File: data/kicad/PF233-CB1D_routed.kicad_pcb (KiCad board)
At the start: 6 copper layers, 78 x 77.2 mm, 62 parts, among them M5 5 V 1.5 A switching module, U1 Pico 2 W

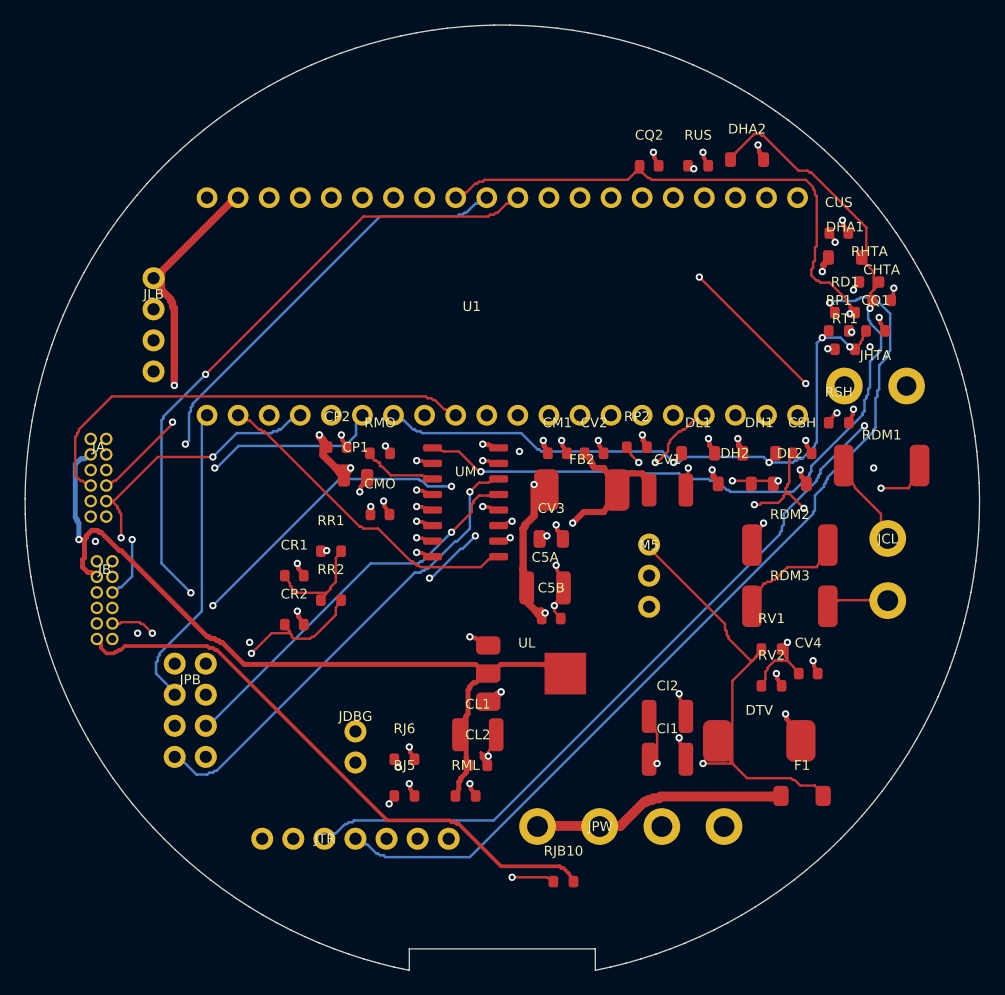
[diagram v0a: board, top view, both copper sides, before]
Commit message: WIP: CB1D-C2 dual-source gyro land (BMI270 / LSM6DSO, pins 2-3 to VDDIO), LSM6DSO datasheet logged, gyro cluster re-placed for escape; CB1D re-route running
Co-Authored-By: Claude Opus 5.5 <noreply@anthropic.com>
Claude-Session: https://claude.ai/code/session_01FX4DWSYYjMCFGGA6gmha65
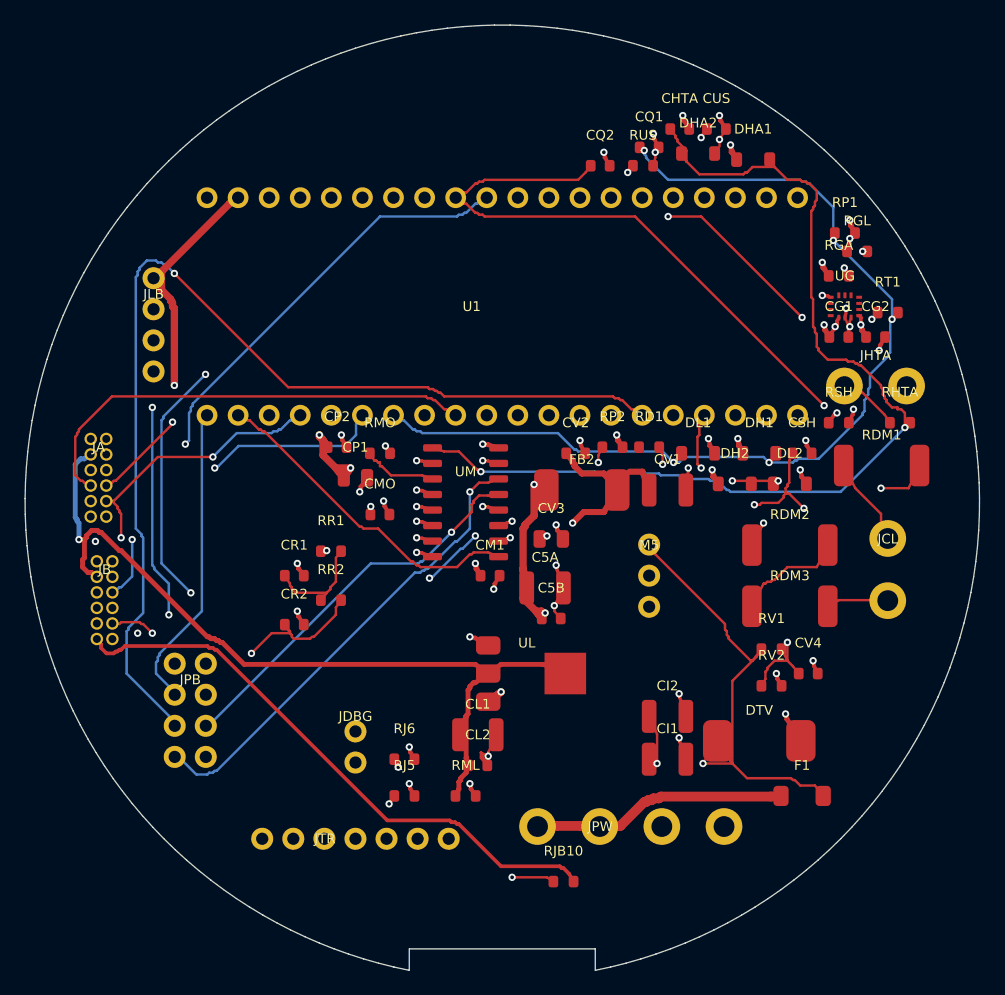
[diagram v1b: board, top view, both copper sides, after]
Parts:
- added CG1: 100n, Capacitor_SMD:C_0603_1608Metric, F.Cu at (127.5, 86.5)
- added CG2: 100n, Capacitor_SMD:C_0603_1608Metric, F.Cu at (130.5, 86.5)
- added RGA: 4k7, Resistor_SMD:R_0603_1608Metric, F.Cu at (127.5, 81.5)
- added RGL: 4k7, Resistor_SMD:R_0603_1608Metric, F.Cu at (129.0, 79.5)
- added UG: BMI270, PF233:BMI270_LGA-14_2.5x3.0mm, F.Cu at (128.0, 84.0)
- moved CQ1 23.8 mm to (112.0, 71.0)
- moved CHTA 21.6 mm to (114.5, 69.5)
- moved RD1 19.4 mm to (112.0, 95.5)
- moved CUS 13.1 mm to (117.5, 69.5)
- moved RHTA 11.8 mm to (132.5, 93.5)
- moved CM1 11.4 mm to (99.0, 106.0)
- moved DHA1 11.0 mm to (120.5, 72.0)
- moved RP1 8.02 mm to (128.0, 78.0)
- moved RT1 4.61 mm to (131.5, 84.5)
- moved RUS 4.50 mm to (111.5, 72.5)
- moved DHA2 4.03 mm to (116.0, 71.5)
- moved CQ2 4.00 mm to (108.0, 72.5)
- moved RP2 2.00 mm to (109.0, 95.5)
- moved CV2 1.50 mm to (106.0, 96.0)
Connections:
- U1 pad 21: (no net) -> GYR_SDA
- U1 pad 22: (no net) -> GYR_SCL
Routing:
- net DIAL_EXT: track 76.1 -> 0.00 mm, vias 1 -> 0
- net FAULT1_N: track 54.9 -> 86.4 mm, vias 3 -> 1
- net TRIG_IN: track 57.5 -> 86.0 mm, vias 4 -> 5
- net UMB_SHLD: track 102.3 -> 88.5 mm, vias 3 -> 4
- net P3V3: track 16.9 -> 29.8 mm, vias 8 -> 12
- net HTA_IN: track 75.1 -> 86.7 mm
- net GYR_SCL: track 0.00 -> 9.61 mm, vias 0 -> 1
- net GYR_SDA: track 0.00 -> 8.76 mm, vias 0 -> 1
- net GND: track 108.7 -> 116.0 mm, vias 39 -> 43
- net TRIG_EXT: track 78.6 -> 85.3 mm, vias 2 -> 1
- net HTA_P: track 10.0 -> 4.92 mm, vias 1 -> 0
- net VBUS_SENSE: track 75.9 -> 79.2 mm, vias 4 -> 3
- net REF_PWM1: track 37.6 -> 39.9 mm
- net +5VA: track 65.5 -> 66.9 mm
- net DIAL_IN: track 77.7 -> 76.4 mm, vias 4 -> 5

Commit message: WIP (NOT signed off): data published by the first close-out sign-off run, which had 5 FAIL (CB1D-C2 / AU1 fine-pitch clearance); superseded by the rerun in progress
Co-Authored-By: Claude Opus 5.5 <noreply@anthropic.com>
Claude-Session: https://claude.ai/code/session_01FX4DWSYYjMCFGGA6gmha65
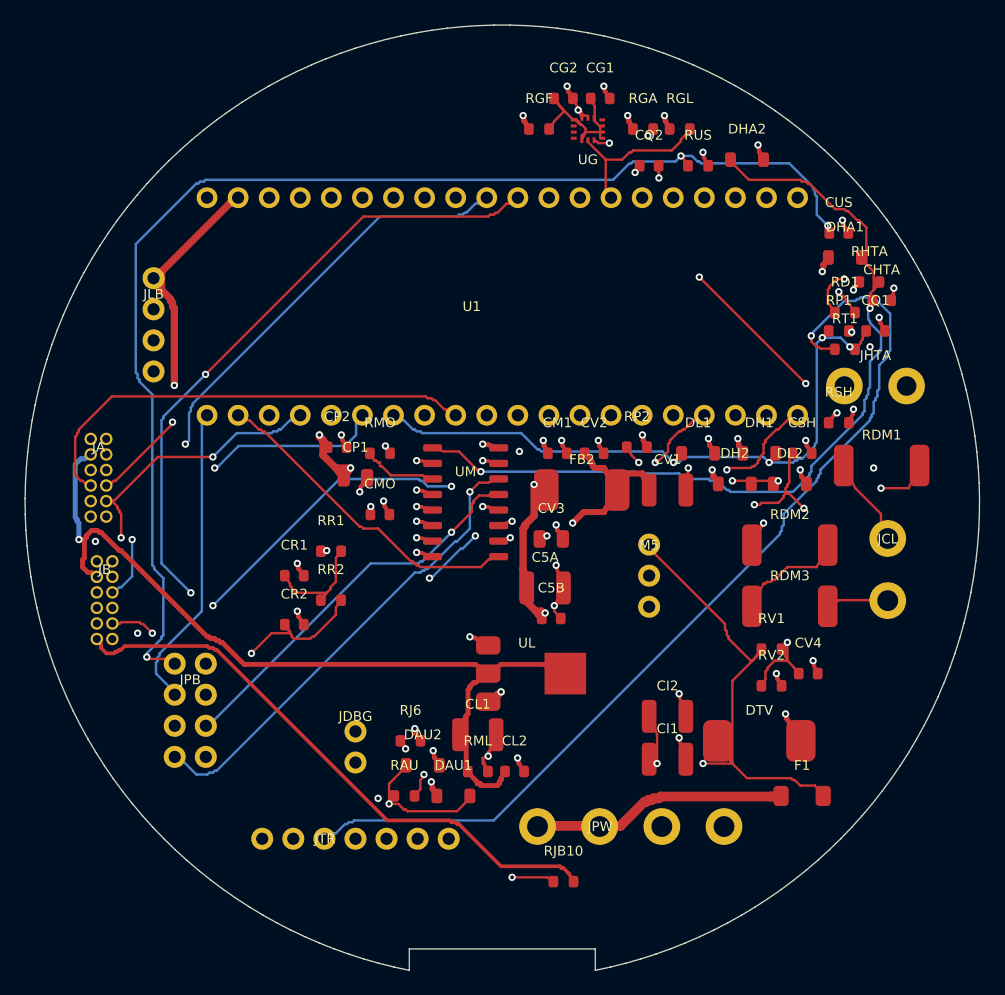
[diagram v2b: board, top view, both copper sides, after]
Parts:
- removed RJ5: 0R DNP, Resistor_SMD:R_0603_1608Metric
- added DAU1: BAS16, Diode_SMD:D_SOD-123, F.Cu at (96.0, 124.0)
- added DAU2: BAS16, Diode_SMD:D_SOD-123, F.Cu at (93.5, 121.5)
- added RAU: 100R, Resistor_SMD:R_0603_1608Metric, F.Cu at (92.0, 124.0)
- added RGF: 10R, Resistor_SMD:R_0603_1608Metric, F.Cu at (103.0, 69.5)
- JTR: value Handle: +3V3 GND TRIG DIAL JOYX JOYY SHLD -> Handle: +3V3 GND TRIG DIAL AUD_LINK - SHLD
- moved CG2 32.1 mm to (105.0, 67.0)
- moved CG1 27.6 mm to (108.0, 67.0)
- moved UG 25.5 mm to (107.0, 69.5), turned to 180 degrees
- moved CQ1 23.8 mm to (130.5, 86.0)
- moved CHTA 21.6 mm to (131.0, 83.5)
- moved RGA 20.0 mm to (111.5, 69.5)
- moved RD1 19.4 mm to (128.0, 84.5)
- moved RGL 17.6 mm to (114.5, 69.5)
- moved CUS 13.1 mm to (127.5, 78.0)
- moved RHTA 11.8 mm to (130.0, 82.0)
- moved CM1 11.4 mm to (104.5, 96.0)
- moved DHA1 11.0 mm to (128.0, 80.0)
- moved RP1 8.02 mm to (127.5, 86.0)
- moved RT1 4.61 mm to (128.0, 87.5)
- moved RUS 4.50 mm to (116.0, 72.5)
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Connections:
- CG1 pad 1: P3V3 -> UG_VIO
- CG2 pad 1: P3V3 -> UG_VIO
- JTR pad 5: JTR5_OPT -> AUD_LINK
- U1 pad 20: (no net) -> AUD_PIO
- U1 pad 21: GYR_SDA -> (no net)
- U1 pad 22: GYR_SCL -> (no net)
- U1 pad 26: (no net) -> GYR_SDA
- U1 pad 27: (no net) -> GYR_SCL
- UG pad 1: GND -> UG_VIO
- UG pad 12: P3V3 -> UG_VIO
- UG pad 2: UG_ASDX_NC -> UG_VIO
- UG pad 3: UG_ASCX_NC -> UG_VIO
- UG pad 5: P3V3 -> UG_VIO
- UG pad 8: P3V3 -> UG_VIO
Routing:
- net DIAL_EXT: track 0.00 -> 76.8 mm, vias 0 -> 2
- net AUD_PIO: track 0.00 -> 46.8 mm, vias 0 -> 2
- net FAULT1_N: track 86.4 -> 54.9 mm, vias 1 -> 3
- net TRIG_IN: track 86.0 -> 57.5 mm, vias 5 -> 4
- net AUD_LINK: track 0.00 -> 17.2 mm, vias 0 -> 1
- net UMB_SHLD: track 88.5 -> 103.9 mm, vias 4 -> 3
- net UG_VIO: track 0.00 -> 13.4 mm
- net HTA_IN: track 86.7 -> 73.4 mm
- net HTA_P: track 4.92 -> 10.0 mm, vias 0 -> 1
- net TRIG_EXT: track 85.3 -> 80.2 mm
- net JTR5_OPT: track 4.47 -> 0.00 mm, vias 1 -> 0
- net GYR_SCL: track 9.61 -> 13.4 mm, vias 1 -> 0
- net VBUS_SENSE: track 79.2 -> 75.9 mm, vias 3 -> 4
- net P3V3: track 29.8 -> 26.7 mm
- net +3V3D: track 72.7 -> 75.0 mm
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
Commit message: WIP (NOT signed off): data published by the second close-out run (8 FAIL: 3 opens on CB1D-C2 / AU1 under the exact fine-zone keep-out); third run in progress
Co-Authored-By: Claude Opus 5.5 <noreply@anthropic.com>
Claude-Session: https://claude.ai/code/session_01FX4DWSYYjMCFGGA6gmha65
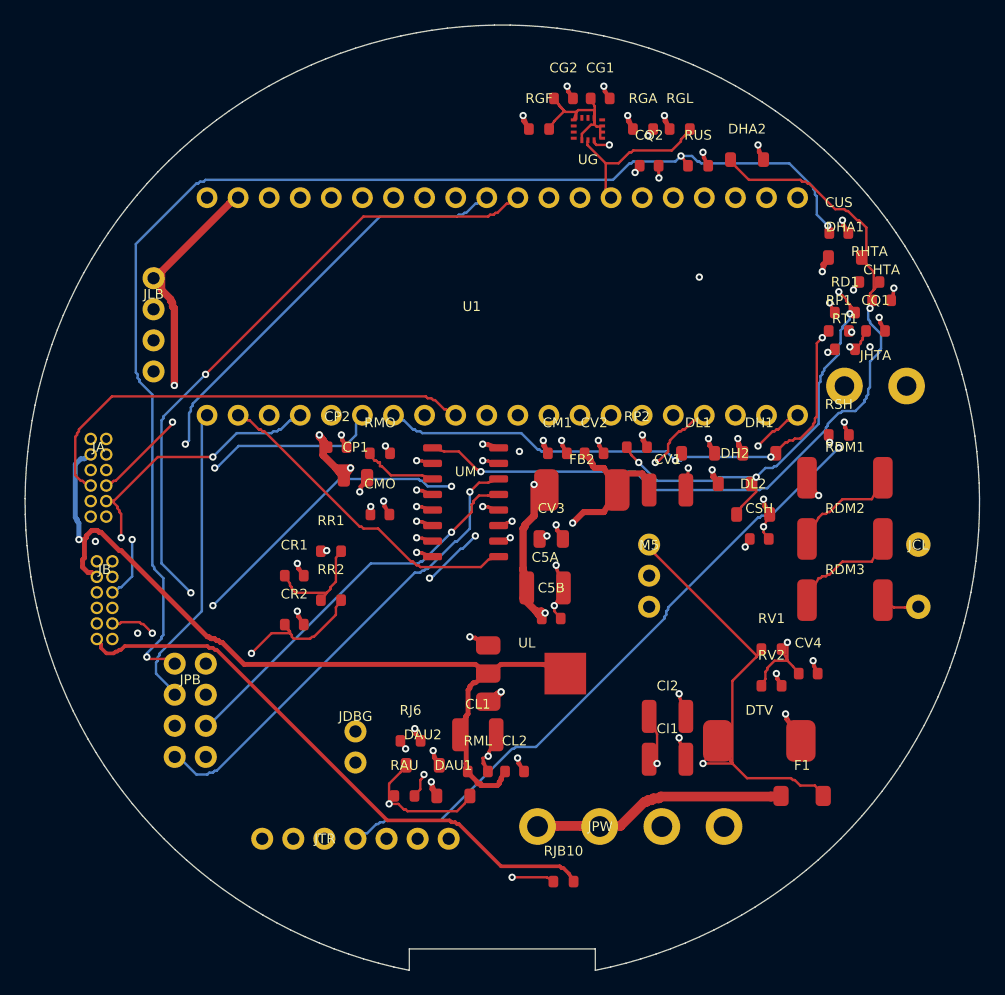
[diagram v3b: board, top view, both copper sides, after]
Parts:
- removed the JCL at (131.5, 105.5)
- removed the JLB at (71.5, 85.5)
- added JCL: Coil taps from TXJ1: COIL_B (drain side), COIL_A (VBUS side), Connector:Solder_holes_AWG22_1x2_P5.08mm, F.Cu at (134.0, 106.0)
- added JLB: to LB1: +5V, LED_IN, LED_CLK, GND, Connector:Wire_pads_1x4_P2.54mm, F.Cu at (71.5, 85.5)
- moved CSH 7.83 mm to (121.0, 103.0)
- moved RDM2 4.53 mm to (128.0, 103.0)
- moved RDM3 4.53 mm to (128.0, 108.0)
- moved DL2 3.91 mm to (120.5, 101.0)
- moved RDM1 3.16 mm to (128.0, 98.0)
- moved RSH 1.00 mm to (127.5, 94.5)
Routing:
- net TRIG_EXT: track 80.2 -> 64.4 mm
- net DM1: track 19.2 -> 8.93 mm, vias 2 -> 0
- net SHIELD: track 57.3 -> 48.3 mm, vias 3 -> 2
- net COIL_B: track 7.16 -> 13.2 mm, vias 0 -> 1
- net DIAL_EXT: track 76.8 -> 71.0 mm
- net GND: track 117.9 -> 114.5 mm, vias 42 -> 41
- net VBUS_SENSE: track 75.9 -> 72.7 mm, vias 4 -> 2
- net TRIG_IN: track 57.5 -> 54.4 mm
- net COIL_A: track 5.03 -> 3.08 mm
- net DIAL_IN: track 78.2 -> 79.9 mm
- net UG_VIO: track 13.4 -> 14.9 mm
- net MUX_S1: track 55.1 -> 54.1 mm
- net MUX_S0: track 53.7 -> 52.7 mm
- net HTA_IN: track 73.4 -> 72.6 mm
- net AUD_PIO: track 46.8 -> 46.1 mm
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
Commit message: WIP (NOT signed off): data written by the close-out runs in progress (fourth run with the 0.15 mm fine-pitch neck-down is running)
Co-Authored-By: Claude Opus 5.5 <noreply@anthropic.com>
Claude-Session: https://claude.ai/code/session_01FX4DWSYYjMCFGGA6gmha65
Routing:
- net GND: track 114.5 -> 117.3 mm, vias 41 -> 42
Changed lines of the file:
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@@
   (gr_line (start 107.600 136.500) (end 92.400 136.500) (stroke (width 0.1) (type default)) (layer "Edge.Cuts"))
   (gr_line (start 92.400 136.500) (end 92.400 138.252) (stroke (width 0.1) (type default)) (layer "Edge.Cuts"))
+  (segment (start 106.9500 68.7000) (end 106.9500 69.3000) (width 0.2) (layer "F.Cu") (net 15))
+  (segment (start 106.9500 69.3000) (end 107.0000 68.5875) (width 0.2) (layer "F.Cu") (net 15))
+  (segment (start 106.5000 68.4000) (end 106.5000 67.9500) (width 0.2) (layer "F.Cu") (net 15))
+  (segment (start 106.5000 67.9500) (end 106.3500 67.8000) (width 0.2) (layer "F.Cu") (net 15))
+  (segment (start 106.3500 67.8000) (end 105.7750 67.0000) (width 0.2) (layer "F.Cu") (net 15))
   (segment (start 108.8900 75.1100) (end 108.4500 74.4000) (width 0.2) (layer "F.Cu") (net 16))
   (segment (start 108.4500 74.4000) (end 108.4500 72.3000) (width 0.2) (layer "F.Cu") (net 16))
@@
   (segment (start 108.0000 69.7500) (end 108.0000 69.3000) (width 0.2) (layer "F.Cu") (net 50))
   (segment (start 108.0000 69.3000) (end 107.7000 69.3000) (width 0.2) (layer "F.Cu") (net 50))
-  (segment (start 107.7000 69.3000) (end 107.5500 69.1500) (width 0.2) (layer "F.Cu") (net 50))
+  (segment (start 107.7000 69.3000) (end 107.7000 69.1500) (width 0.2) (layer "F.Cu") (net 50))
+  (segment (start 107.7000 69.1500) (end 107.5500 69.1500) (width 0.2) (layer "F.Cu") (net 50))
   (segment (start 107.5500 69.1500) (end 107.5500 68.7000) (width 0.2) (layer "F.Cu") (net 50))
   (segment (start 107.5500 68.7000) (end 107.5500 67.6500) (width 0.2) (layer "F.Cu") (net 50))
   (segment (start 107.5500 67.6500) (end 107.2250 67.0000) (width 0.2) (layer "F.Cu") (net 50))
-  (segment (start 107.5000 68.5875) (end 107.5500 69.1500) (width 0.2) (layer "F.Cu") (net 50))
-  (segment (start 107.5500 69.1500) (end 107.2500 69.1500) (width 0.2) (layer "F.Cu") (net 50))
-  (segment (start 107.2500 69.1500) (end 106.5000 69.9000) (width 0.2) (layer "F.Cu") (net 50))
-  (segment (start 106.5000 69.9000) (end 106.5000 70.2000) (width 0.2) (layer "F.Cu") (net 50))
-  (segment (start 107.5000 68.5875) (end 107.5500 67.9500) (width 0.2) (layer "F.Cu") (net 50))
-  (segment (start 107.5500 67.9500) (end 106.2000 67.9500) (width 0.2) (layer "F.Cu") (net 50))
-  (segment (start 106.2000 67.9500) (end 106.0500 68.1000) (width 0.2) (layer "F.Cu") (net 50))
-  (segment (start 106.0500 68.1000) (end 106.0500 68.7000) (width 0.2) (layer "F.Cu") (net 50))
-  (segment (start 105.8375 68.7500) (end 106.0500 68.1000) (width 0.2) (layer "F.Cu") (net 50))
-  (segment (start 106.0500 68.1000) (end 105.1500 68.1000) (width 0.2) (layer "F.Cu") (net 50))
-  (segment (start 105.1500 68.1000) (end 104.7000 67.6500) (width 0.2) (layer "F.Cu") (net 50))
-  (segment (start 104.7000 67.6500) (end 104.2250 67.0000) (width 0.2) (layer "F.Cu") (net 50))
-  (segment (start 104.2250 67.0000) (end 105.0000 67.9500) (width 0.2) (layer "F.Cu") (net 50))
-  (segment (start 105.0000 67.9500) (end 105.0000 68.1000) (width 0.2) (layer "F.Cu") (net 50))
-  (segment (start 105.0000 68.1000) (end 104.2500 68.8500) (width 0.2) (layer "F.Cu") (net 50))
+  (segment (start 107.2250 67.0000) (end 107.5500 67.6500) (width 0.2) (layer "F.Cu") (net 50))
+  (segment (start 107.5500 67.6500) (end 107.5500 66.9000) (width 0.2) (layer "F.Cu") (net 50))
+  (segment (start 107.5500 66.9000) (end 106.6500 66.0000) (width 0.2) (layer "F.Cu") (net 50))
+  (segment (start 106.6500 66.0000) (end 106.5000 66.0000) (width 0.2) (layer "F.Cu") (net 50))
+  (segment (start 106.5000 66.0000) (end 106.3500 65.8500) (width 0.2) (layer "F.Cu") (net 50))
+  (segment (start 106.3500 65.8500) (end 105.0000 65.8500) (width 0.2) (layer "F.Cu") (net 50))
+  (segment (start 105.0000 65.8500) (end 104.8500 66.0000) (width 0.2) (layer "F.Cu") (net 50))
+  (segment (start 104.8500 66.0000) (end 104.8500 66.1500) (width 0.2) (layer "F.Cu") (net 50))
+  (segment (start 104.8500 66.1500) (end 104.7000 66.3000) (width 0.2) (layer "F.Cu") (net 50))
+  (segment (start 104.7000 66.3000) (end 104.7000 66.4500) (width 0.2) (layer "F.Cu") (net 50))
+  (segment (start 104.7000 66.4500) (end 104.2250 67.0000) (width 0.2) (layer "F.Cu") (net 50))
+  (segment (start 104.2250 67.0000) (end 104.7000 66.4500) (width 0.2) (layer "F.Cu") (net 50))
+  (segment (start 104.7000 66.4500) (end 104.7000 68.4000) (width 0.2) (layer "F.Cu") (net 50))
+  (segment (start 104.7000 68.4000) (end 104.2500 68.8500) (width 0.2) (layer "F.Cu") (net 50))
   (segment (start 104.2500 68.8500) (end 103.8250 69.5000) (width 0.2) (layer "F.Cu") (net 50))
+  (segment (start 104.7000 68.4000) (end 105.4500 68.4000) (width 0.2) (layer "F.Cu") (net 50))
+  (segment (start 105.4500 68.4000) (end 105.7500 68.7000) (width 0.2) (layer "F.Cu") (net 50))
   (segment (start 88.9500 98.0000) (end 88.3500 98.7000) (width 0.2) (layer "F.Cu") (net 15))
   (segment (start 88.3500 98.7000) (end 88.3500 99.1500) (width 0.2) (layer "F.Cu") (net 15))
@@
   (segment (start 108.3000 66.4500) (end 108.3000 66.0000) (width 0.2) (layer "F.Cu") (net 15))
   (segment (start 108.3000 66.0000) (end 108.7750 67.0000) (width 0.2) (layer "F.Cu") (net 15))
-  (segment (start 105.7750 67.0000) (end 105.3000 66.4500) (width 0.2) (layer "F.Cu") (net 15))
-  (segment (start 105.3000 66.4500) (end 105.3000 66.0000) (width 0.2) (layer "F.Cu") (net 15))
-  (segment (start 105.3000 66.0000) (end 105.7750 67.0000) (width 0.2) (layer "F.Cu") (net 15))
+  (segment (start 105.7750 67.0000) (end 106.2000 67.6500) (width 0.2) (layer "F.Cu") (net 15))
+  (segment (start 106.2000 67.6500) (end 106.2000 68.1000) (width 0.2) (layer "F.Cu") (net 15))
+  (segment (start 106.2000 68.1000) (end 106.5000 68.5875) (width 0.2) (layer "F.Cu") (net 15))
   (segment (start 99.7000 95.5550) (end 98.8500 95.2500) (width 0.3) (layer "F.Cu") (net 31))
   (segment (start 98.8500 95.2500) (end 98.4000 95.2500) (width 0.3) (layer "F.Cu") (net 31))
@@
   (segment (start 126.6000 77.4000) (end 126.7250 78.0000) (width 0.2) (layer "F.Cu") (net 51))
   (segment (start 98.4000 120.9000) (end 98.8500 120.7500) (width 0.2) (layer "F.Cu") (net 15))
+  (segment (start 106.2000 68.1000) (end 106.3500 67.8000) (width 0.2) (layer "F.Cu") (net 15))
   (segment (start 111.0000 73.0500) (end 110.8500 73.0500) (width 0.2) (layer "F.Cu") (net 11))
   (segment (start 111.0000 73.0500) (end 110.8500 73.0500) (width 0.2) (layer "In3.Cu") (net 11))
+  (via (at 106.9500 69.3000) (size 0.6) (drill 0.3) (layers "F.Cu" "B.Cu") (net 15))
+  (via (at 106.3500 67.8000) (size 0.6) (drill 0.3) (layers "F.Cu" "B.Cu") (net 15))
   (via (at 111.9000 70.0500) (size 0.6) (drill 0.3) (layers "F.Cu" "B.Cu") (net 17))
   (via (at 108.7500 70.8000) (size 0.6) (drill 0.3) (layers "F.Cu" "B.Cu") (net 17))
@@
   (via (at 120.9000 70.8000) (size 0.6) (drill 0.3) (layers "F.Cu" "B.Cu") (net 15))
   (via (at 108.3000 66.0000) (size 0.6) (drill 0.3) (layers "F.Cu" "B.Cu") (net 15))
-  (via (at 105.3000 66.0000) (size 0.6) (drill 0.3) (layers "F.Cu" "B.Cu") (net 15))
   (via (at 98.4000 95.2500) (size 0.6) (drill 0.3) (layers "F.Cu" "B.Cu") (net 31))
   (via (at 103.3500 94.9500) (size 0.6) (drill 0.3) (layers "F.Cu" "B.Cu") (net 31))
